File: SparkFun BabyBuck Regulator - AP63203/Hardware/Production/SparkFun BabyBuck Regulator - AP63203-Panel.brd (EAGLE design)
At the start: 151.6 x 179.6 mm, 3156 parts, among them U1 AP63203, U10 AP63203, U100 AP63203, U101 AP63203, U102 AP63203, U103 AP63203, U104 AP63203, U105 AP63203, U106 AP63203, U107 AP63203, U108 AP63203, U109 AP63203, U11 AP63203, U110 AP63203, U111 AP63203, U112 AP63203, U113 AP63203, U114 AP63203, U115 AP63203, U116 AP63203, U117 AP63203, U118 AP63203, U119 AP63203, U12 AP63203, U120 AP63203, U121 AP63203, U122 AP63203, U123 AP63203, U124 AP63203, U125 AP63203, U126 AP63203, U127 AP63203, U128 AP63203, U129 AP63203, U13 AP63203, U130 AP63203, U131 AP63203, U132 AP63203, U133 AP63203, U134 AP63203, U135 AP63203, U136 AP63203, U137 AP63203, U138 AP63203, U139 AP63203, U14 AP63203, U140 AP63203, U141 AP63203, U142 AP63203, U143 AP63203, U144 AP63203, U145 AP63203, U146 AP63203, U147 AP63203, U148 AP63203, U149 AP63203, U15 AP63203, U150 AP63203, U16 AP63203, U17 AP63203, U18 AP63203, U19 AP63203, U2 AP63203, U20 AP63203, U21 AP63203, U22 AP63203, U23 AP63203, U24 AP63203, U25 AP63203, U26 AP63203, U27 AP63203, U28 AP63203, U29 AP63203, U3 AP63203, U30 AP63203, U31 AP63203, U32 AP63203, U33 AP63203, U34 AP63203, U35 AP63203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

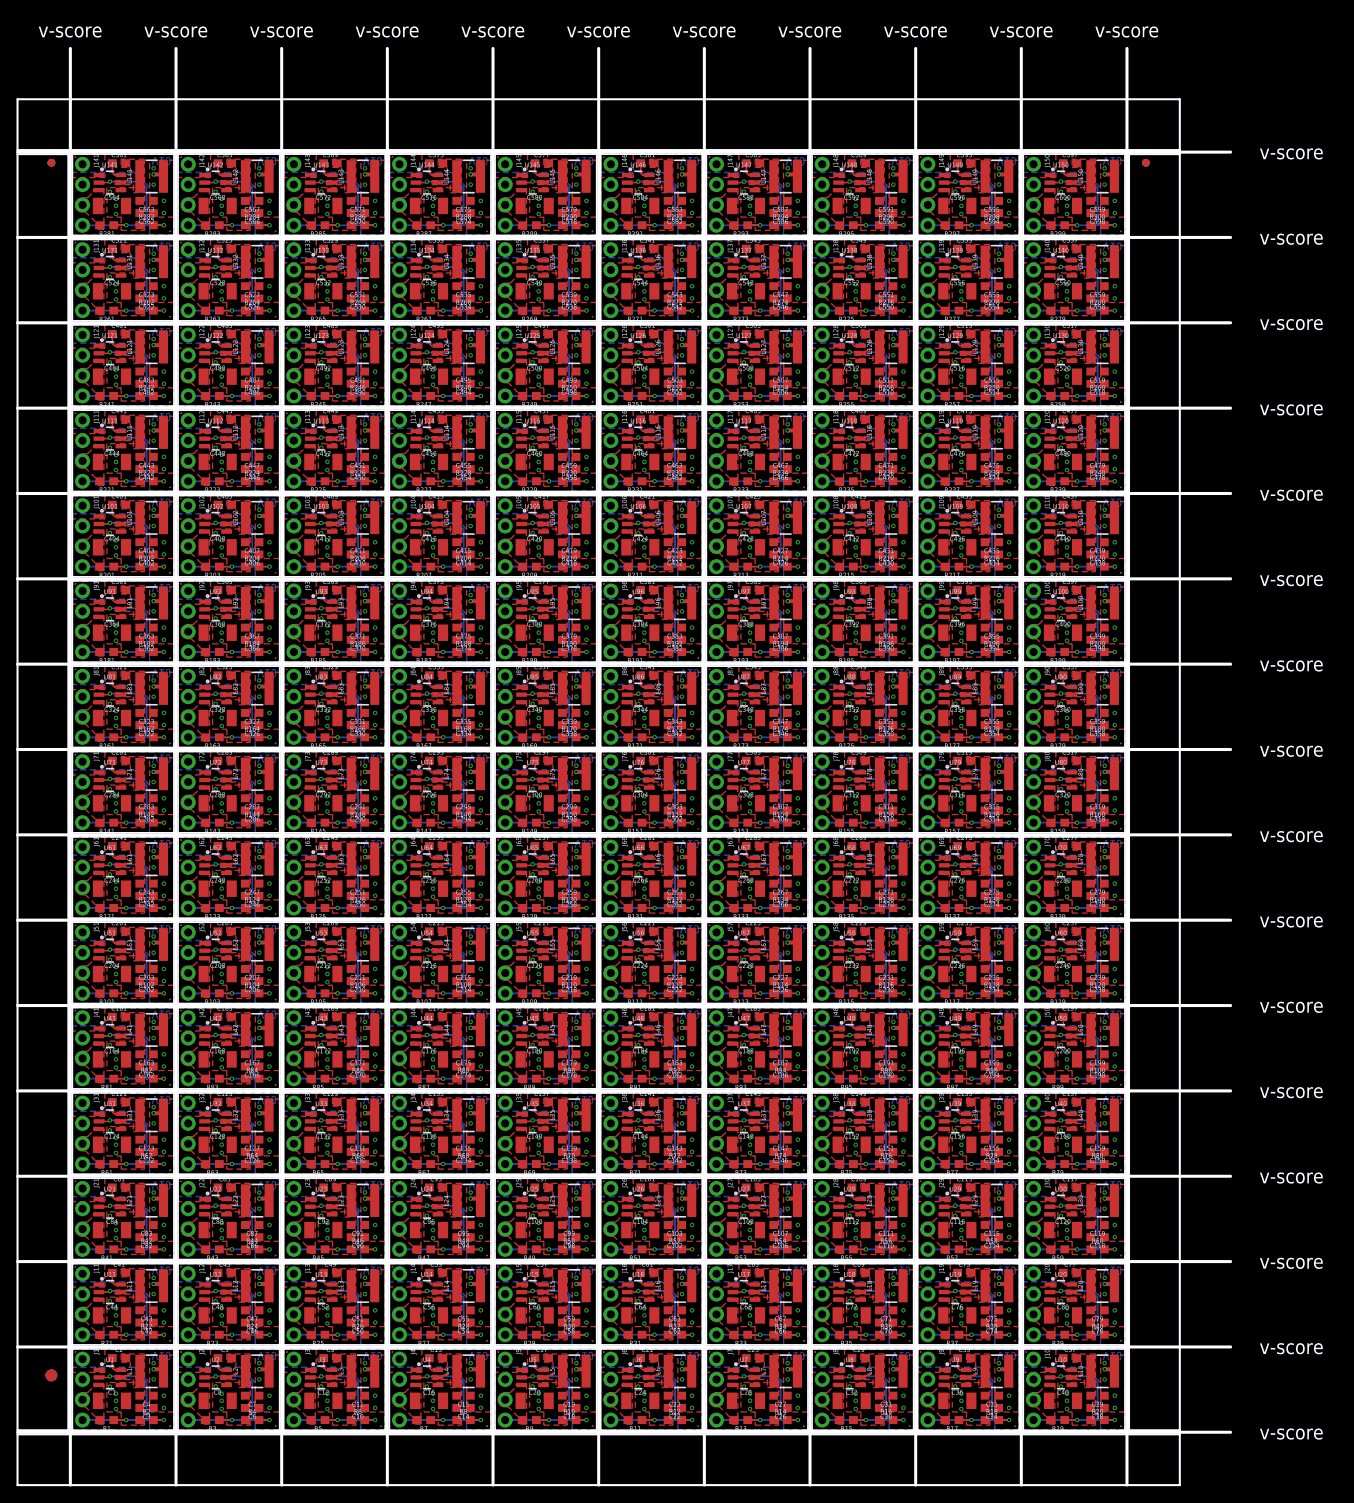
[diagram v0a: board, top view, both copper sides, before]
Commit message: BabyBuck Panel Update
Reduced panel size
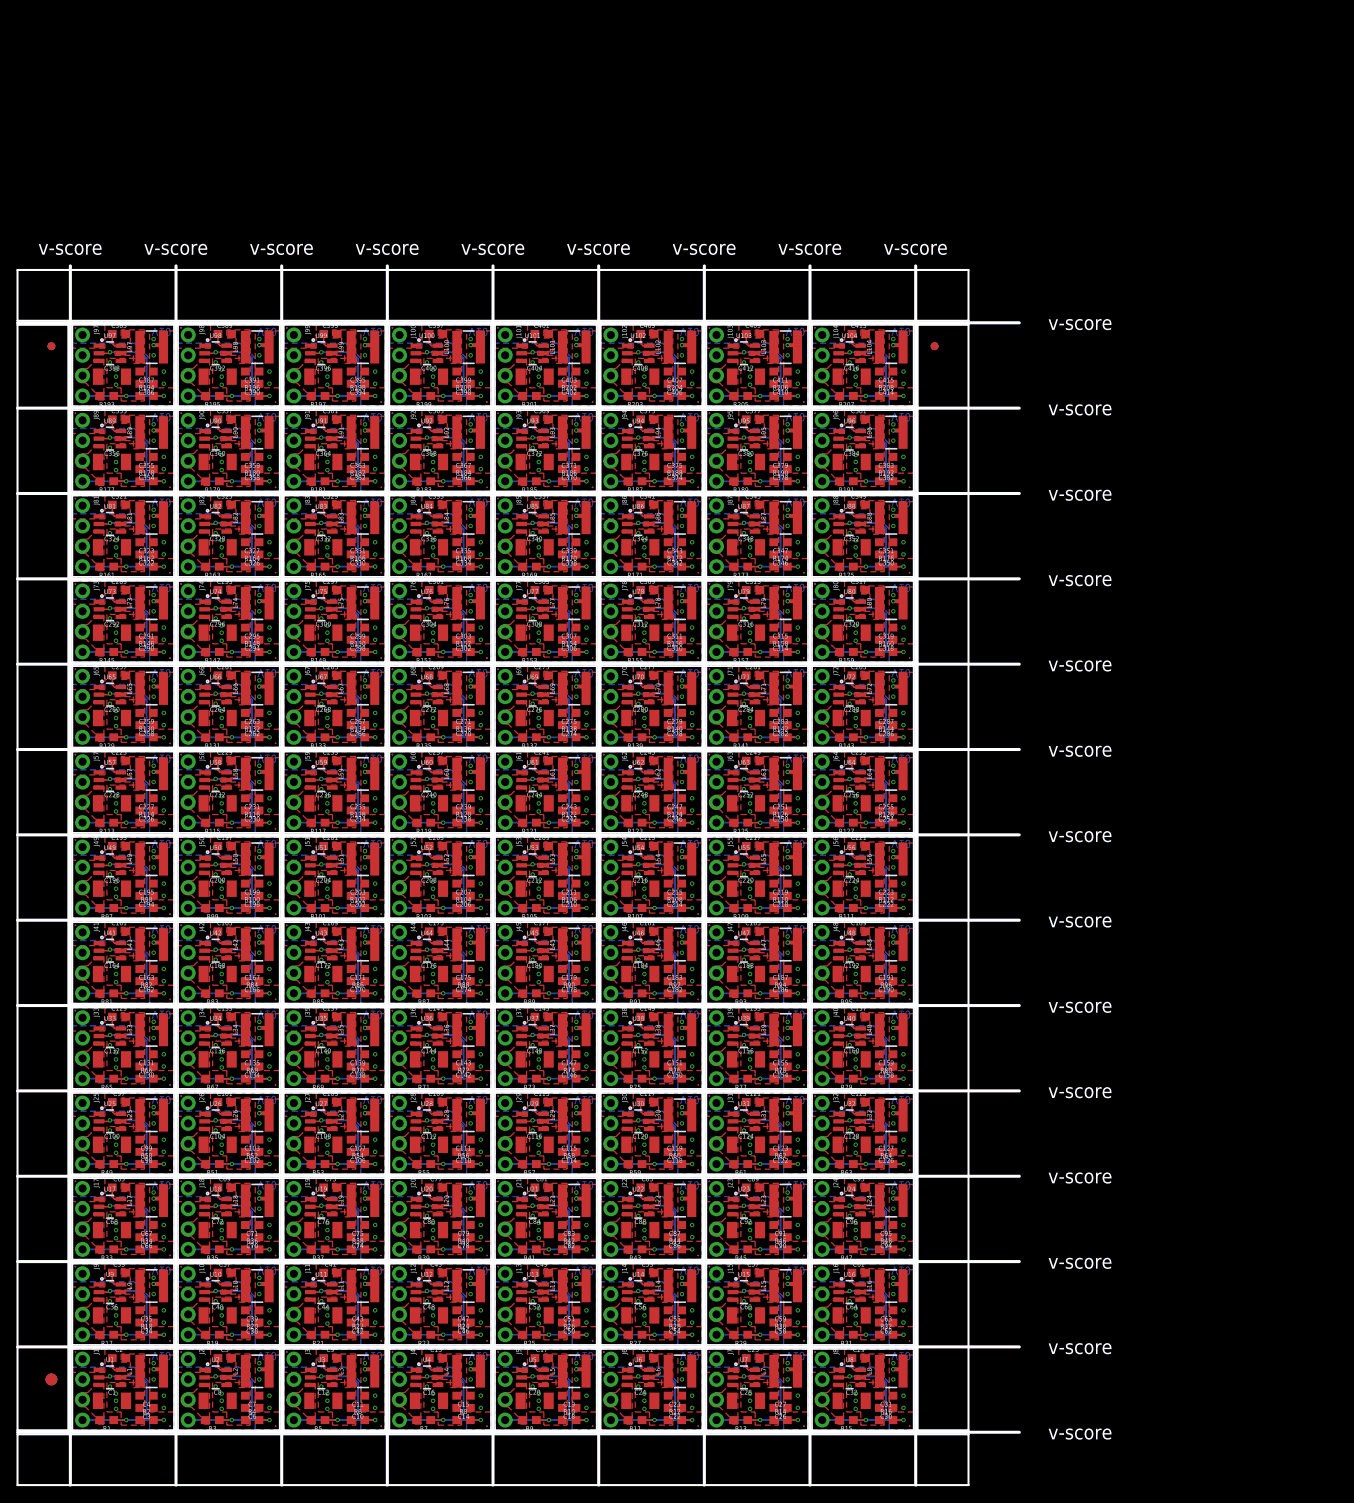
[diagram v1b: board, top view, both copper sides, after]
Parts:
- removed C417, C421, C425, C429, C433, C437, C441, C445, C449, C453, C457, C461, C465, C469, C473, C477, C481, C485, C489, C493, C497, C501, C505, C509, C513, C517, C521, C525, C529, C533, C537, C541, C545, C549, C553, C557, C561, C565, C569, C573, C577, C581, C585, C589, C593, C597: 0.1uF, SparkFun-Capacitors:0603
- removed C418, C419, C422, C423, C426, C427, C430, C431, C434, C435, C438, C439, C442, C443, C446, C447, C450, C451, C454, C455, C458, C459, C462, C463, C466, C467, C470, C471, C474, C475, C478, C479, C482, C483, C486, C487, C490, C491, C494, C495, C498, C499, C502, C503, C506, C507, C510, C511, C514, C515, C518, C519, C522, C523, C526, C527, C530, C531, C534, C535, C538, C539, C542, C543, C546, C547, C550, C551, C554, C555, C558, C559, C562, C563, C566, C567, C570, C571, C574, C575, C578, C579, C582, C583, C586, C587, C590, C591, C594, C595, C598, C599: 22uF, SparkFun-Capacitors:0603
- removed C420, C424, C428, C432, C436, C440, C444, C448, C452, C456, C460, C464, C468, C472, C476, C480, C484, C488, C492, C496, C500, C504, C508, C512, C516, C520, C524, C528, C532, C536, C540, C544, C548, C552, C556, C560, C564, C568, C572, C576, C580, C584, C588, C592, C596, C600: 10uF, SparkFun-Capacitors:1210
- removed FD417, FD418, FD419, FD420, FD421, FD422, FD423, FD424, FD425, FD426, FD427, FD428, FD429, FD430, FD431, FD432, FD433, FD434, FD435, FD436, FD437, FD438, FD439, FD440, FD441, FD442, FD443, FD444, FD445, FD446, FD447, FD448, FD449, FD450, FD451, FD452, FD453, FD454, FD455, FD456, FD457, FD458, FD459, FD460, FD461, FD462, FD463, FD464, FD465, FD466, FD467, FD468, FD469, FD470, FD471, FD472, FD473, FD474, FD475, FD476, FD477, FD478, FD479, FD480, FD481, FD482, FD483, FD484, FD485, FD486, FD487, FD488, FD489, FD490, FD491, FD492, FD493, FD494, FD495, FD496, FD497, FD498, FD499, FD500, FD501, FD502, FD503, FD504, FD505, FD506, FD507, FD508, FD509, FD510, FD511, FD512, FD513, FD514, FD515, FD516, FD517, FD518, FD519, FD520, FD521, FD522, FD523, FD524, FD525, FD526, FD527, FD528, FD529, FD530, FD531, FD532, FD533, FD534, FD535, FD536, FD537, FD538, FD539, FD540, FD541, FD542, FD543, FD544, FD545, FD546, FD547, FD548, FD549, FD550, FD551, FD552, FD553, FD554, FD555, FD556, FD557, FD558, FD559, FD560, FD561, FD562, FD563, FD564, FD565, FD566, FD567, FD568, FD569, FD570, FD571, FD572, FD573, FD574, FD575, FD576, FD577, FD578, FD579, FD580, FD581, FD582, FD583, FD584, FD585, FD586, FD587, FD588, FD589, FD590, FD591, FD592, FD593, FD594, FD595, FD596, FD597, FD598, FD599, FD600: FIDUCIAL0.2MM, SparkFun-Aesthetics:FIDUCIAL-0.2MM
- removed J105, J106, J107, J108, J109, J110, J111, J112, J113, J114, J115, J116, J117, J118, J119, J120, J121, J122, J123, J124, J125, J126, J127, J128, J129, J130, J131, J132, J133, J134, J135, J136, J137, J138, J139, J140, J141, J142, J143, J144, J145, J146, J147, J148, J149, J150: (no value), SparkFun-Connectors:1X04_NO_SILK
- removed L105, L106, L107, L108, L109, L110, L111, L112, L113, L114, L115, L116, L117, L118, L119, L120, L121, L122, L123, L124, L125, L126, L127, L128, L129, L130, L131, L132, L133, L134, L135, L136, L137, L138, L139, L140, L141, L142, L143, L144, L145, L146, L147, L148, L149, L150: 4.7μH, SparkFun-Coils:INDUCTOR_4X4MM
- removed LOGO209, LOGO211, LOGO213, LOGO215, LOGO217, LOGO219, LOGO221, LOGO223, LOGO225, LOGO227, LOGO229, LOGO231, LOGO233, LOGO235, LOGO237, LOGO239, LOGO241, LOGO243, LOGO245, LOGO247, LOGO249, LOGO251, LOGO253, LOGO255, LOGO257, LOGO259, LOGO261, LOGO263, LOGO265, LOGO267, LOGO269, LOGO271, LOGO273, LOGO275, LOGO277, LOGO279, LOGO281, LOGO283, LOGO285, LOGO287, LOGO289, LOGO291, LOGO293, LOGO295, LOGO297, LOGO299: SFE_LOGO_FLAME.1_INCH, SparkFun-Aesthetics:SFE_LOGO_FLAME_.1
- removed LOGO210, LOGO212, LOGO214, LOGO216, LOGO218, LOGO220, LOGO222, LOGO224, LOGO226, LOGO228, LOGO230, LOGO232, LOGO234, LOGO236, LOGO238, LOGO240, LOGO242, LOGO244, LOGO246, LOGO248, LOGO250, LOGO252, LOGO254, LOGO256, LOGO258, LOGO260, LOGO262, LOGO264, LOGO266, LOGO268, LOGO270, LOGO272, LOGO274, LOGO276, LOGO278, LOGO280, LOGO282, LOGO284, LOGO286, LOGO288, LOGO290, LOGO292, LOGO294, LOGO296, LOGO298, LOGO300: OSHW-LOGOS, SparkFun-Aesthetics:OSHW-LOGO-S
- removed R209, R210, R211, R212, R213, R214, R215, R216, R217, R218, R219, R220, R221, R222, R223, R224, R225, R226, R227, R228, R229, R230, R231, R232, R233, R234, R235, R236, R237, R238, R239, R240, R241, R242, R243, R244, R245, R246, R247, R248, R249, R250, R251, R252, R253, R254, R255, R256, R257, R258, R259, R260, R261, R262, R263, R264, R265, R266, R267, R268, R269, R270, R271, R272, R273, R274, R275, R276, R277, R278, R279, R280, R281, R282, R283, R284, R285, R286, R287, R288, R289, R290, R291, R292, R293, R294, R295, R296, R297, R298, R299, R300: 100k, SparkFun-Resistors:0603
- removed U$625, U$631, U$637, U$643, U$649, U$655, U$661, U$667, U$673, U$679, U$685, U$691, U$697, U$703, U$709, U$715, U$721, U$727, U$733, U$739, U$745, U$751, U$757, U$763, U$769, U$775, U$781, U$787, U$793, U$799, U$805, U$811, U$817, U$823, U$829, U$835, U$841, U$847, U$853, U$859, U$865, U$871, U$877, U$883, U$889, U$895: (no value), output:#3V3#0
- removed U$626, U$632, U$638, U$644, U$650, U$656, U$662, U$668, U$674, U$680, U$686, U$692, U$698, U$704, U$710, U$716, U$722, U$728, U$734, U$740, U$746, U$752, U$758, U$764, U$770, U$776, U$782, U$788, U$794, U$800, U$806, U$812, U$818, U$824, U$830, U$836, U$842, U$848, U$854, U$860, U$866, U$872, U$878, U$884, U$890, U$896: (no value), output:#GND#0
- removed U$627, U$633, U$639, U$645, U$651, U$657, U$663, U$669, U$675, U$681, U$687, U$693, U$699, U$705, U$711, U$717, U$723, U$729, U$735, U$741, U$747, U$753, U$759, U$765, U$771, U$777, U$783, U$789, U$795, U$801, U$807, U$813, U$819, U$825, U$831, U$837, U$843, U$849, U$855, U$861, U$867, U$873, U$879, U$885, U$891, U$897: (no value), output:#EN#0
- removed U$628, U$634, U$640, U$646, U$652, U$658, U$664, U$670, U$676, U$682, U$688, U$694, U$700, U$706, U$712, U$718, U$724, U$730, U$736, U$742, U$748, U$754, U$760, U$766, U$772, U$778, U$784, U$790, U$796, U$802, U$808, U$814, U$820, U$826, U$832, U$838, U$844, U$850, U$856, U$862, U$868, U$874, U$880, U$886, U$892, U$898: (no value), output:#VIN#0
- removed U$629, U$635, U$641, U$647, U$653, U$659, U$665, U$671, U$677, U$683, U$689, U$695, U$701, U$707, U$713, U$719, U$725, U$731, U$737, U$743, U$749, U$755, U$761, U$767, U$773, U$779, U$785, U$791, U$797, U$803, U$809, U$815, U$821, U$827, U$833, U$839, U$845, U$851, U$857, U$863, U$869, U$875, U$881, U$887, U$893, U$899: (no value), output:AP632030
- removed U$630, U$636, U$642, U$648, U$654, U$660, U$666, U$672, U$678, U$684, U$690, U$696, U$702, U$708, U$714, U$720, U$726, U$732, U$738, U$744, U$750, U$756, U$762, U$768, U$774, U$780, U$786, U$792, U$798, U$804, U$810, U$816, U$822, U$828, U$834, U$840, U$846, U$852, U$858, U$864, U$870, U$876, U$882, U$888, U$894, U$900: (no value), output:BABYBUCK0
- removed U105, U106, U107, U108, U109, U110, U111, U112, U113, U114, U115, U116, U117, U118, U119, U120, U121, U122, U123, U124, U125, U126, U127, U128, U129, U130, U131, U132, U133, U134, U135, U136, U137, U138, U139, U140, U141, U142, U143, U144, U145, U146, U147, U148, U149, U150: AP63203, SparkFun-IC-Power:SOT23-6
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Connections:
- removed net 3.3V104: C418.1, C419.1, J105.1, L105.P$2, U105.1
- removed net 3.3V105: C422.1, C423.1, J106.1, L106.P$2, U106.1
- removed net 3.3V106: C426.1, C427.1, J107.1, L107.P$2, U107.1
- removed net 3.3V107: C430.1, C431.1, J108.1, L108.P$2, U108.1
- removed net 3.3V108: C434.1, C435.1, J109.1, L109.P$2, U109.1
- removed net 3.3V109: C438.1, C439.1, J110.1, L110.P$2, U110.1
- removed net 3.3V110: C442.1, C443.1, J111.1, L111.P$2, U111.1
- removed net 3.3V111: C446.1, C447.1, J112.1, L112.P$2, U112.1
- removed net 3.3V112: C450.1, C451.1, J113.1, L113.P$2, U113.1
- removed net 3.3V113: C454.1, C455.1, J114.1, L114.P$2, U114.1
- removed net 3.3V114: C458.1, C459.1, J115.1, L115.P$2, U115.1
- removed net 3.3V115: C462.1, C463.1, J116.1, L116.P$2, U116.1
- removed net 3.3V116: C466.1, C467.1, J117.1, L117.P$2, U117.1
- removed net 3.3V117: C470.1, C471.1, J118.1, L118.P$2, U118.1
- removed net 3.3V118: C474.1, C475.1, J119.1, L119.P$2, U119.1
- removed net 3.3V119: C478.1, C479.1, J120.1, L120.P$2, U120.1
- removed net 3.3V120: C482.1, C483.1, J121.1, L121.P$2, U121.1
- removed net 3.3V121: C486.1, C487.1, J122.1, L122.P$2, U122.1
- removed net 3.3V122: C490.1, C491.1, J123.1, L123.P$2, U123.1
- removed net 3.3V123: C494.1, C495.1, J124.1, L124.P$2, U124.1
- removed net 3.3V124: C498.1, C499.1, J125.1, L125.P$2, U125.1
- removed net 3.3V125: C502.1, C503.1, J126.1, L126.P$2, U126.1
- removed net 3.3V126: C506.1, C507.1, J127.1, L127.P$2, U127.1
- removed net 3.3V127: C510.1, C511.1, J128.1, L128.P$2, U128.1
- removed net 3.3V128: C514.1, C515.1, J129.1, L129.P$2, U129.1
- removed net 3.3V129: C518.1, C519.1, J130.1, L130.P$2, U130.1
- removed net 3.3V130: C522.1, C523.1, J131.1, L131.P$2, U131.1
- removed net 3.3V131: C526.1, C527.1, J132.1, L132.P$2, U132.1
- removed net 3.3V132: C530.1, C531.1, J133.1, L133.P$2, U133.1
- removed net 3.3V133: C534.1, C535.1, J134.1, L134.P$2, U134.1
- removed net 3.3V134: C538.1, C539.1, J135.1, L135.P$2, U135.1
- removed net 3.3V135: C542.1, C543.1, J136.1, L136.P$2, U136.1
- removed net 3.3V136: C546.1, C547.1, J137.1, L137.P$2, U137.1
- removed net 3.3V137: C550.1, C551.1, J138.1, L138.P$2, U138.1
- removed net 3.3V138: C554.1, C555.1, J139.1, L139.P$2, U139.1
- removed net 3.3V139: C558.1, C559.1, J140.1, L140.P$2, U140.1
- removed net 3.3V140: C562.1, C563.1, J141.1, L141.P$2, U141.1
- removed net 3.3V141: C566.1, C567.1, J142.1, L142.P$2, U142.1
- removed net 3.3V142: C570.1, C571.1, J143.1, L143.P$2, U143.1
- removed net 3.3V143: C574.1, C575.1, J144.1, L144.P$2, U144.1
- removed net 3.3V144: C578.1, C579.1, J145.1, L145.P$2, U145.1
- removed net 3.3V145: C582.1, C583.1, J146.1, L146.P$2, U146.1
- removed net 3.3V146: C586.1, C587.1, J147.1, L147.P$2, U147.1
- removed net 3.3V147: C590.1, C591.1, J148.1, L148.P$2, U148.1
- removed net 3.3V148: C594.1, C595.1, J149.1, L149.P$2, U149.1
- removed net 3.3V149: C598.1, C599.1, J150.1, L150.P$2, U150.1
- removed net EN104: J105.4, R209.1, R210.2, U105.2
- removed net EN105: J106.4, R211.1, R212.2, U106.2
- removed net EN106: J107.4, R213.1, R214.2, U107.2
- removed net EN107: J108.4, R215.1, R216.2, U108.2
- removed net EN108: J109.4, R217.1, R218.2, U109.2
- removed net EN109: J110.4, R219.1, R220.2, U110.2
- removed net EN110: J111.4, R221.1, R222.2, U111.2
- removed net EN111: J112.4, R223.1, R224.2, U112.2
- removed net EN112: J113.4, R225.1, R226.2, U113.2
- removed net EN113: J114.4, R227.1, R228.2, U114.2
- removed net EN114: J115.4, R229.1, R230.2, U115.2
- removed net EN115: J116.4, R231.1, R232.2, U116.2
- removed net EN116: J117.4, R233.1, R234.2, U117.2
- removed net EN117: J118.4, R235.1, R236.2, U118.2
- removed net EN118: J119.4, R237.1, R238.2, U119.2
- removed net EN119: J120.4, R239.1, R240.2, U120.2
- removed net EN120: J121.4, R241.1, R242.2, U121.2
- removed net EN121: J122.4, R243.1, R244.2, U122.2
- removed net EN122: J123.4, R245.1, R246.2, U123.2
- removed net EN123: J124.4, R247.1, R248.2, U124.2
- removed net EN124: J125.4, R249.1, R250.2, U125.2
- removed net EN125: J126.4, R251.1, R252.2, U126.2
- removed net EN126: J127.4, R253.1, R254.2, U127.2
- removed net EN127: J128.4, R255.1, R256.2, U128.2
- removed net EN128: J129.4, R257.1, R258.2, U129.2
- removed net EN129: J130.4, R259.1, R260.2, U130.2
- removed net EN130: J131.4, R261.1, R262.2, U131.2
- removed net EN131: J132.4, R263.1, R264.2, U132.2
- removed net EN132: J133.4, R265.1, R266.2, U133.2
- removed net EN133: J134.4, R267.1, R268.2, U134.2
- removed net EN134: J135.4, R269.1, R270.2, U135.2
- removed net EN135: J136.4, R271.1, R272.2, U136.2
- removed net EN136: J137.4, R273.1, R274.2, U137.2
- removed net EN137: J138.4, R275.1, R276.2, U138.2
- removed net EN138: J139.4, R277.1, R278.2, U139.2
- removed net EN139: J140.4, R279.1, R280.2, U140.2
- removed net EN140: J141.4, R281.1, R282.2, U141.2
- removed net EN141: J142.4, R283.1, R284.2, U142.2
- removed net EN142: J143.4, R285.1, R286.2, U143.2
- removed net EN143: J144.4, R287.1, R288.2, U144.2
- removed net EN144: J145.4, R289.1, R290.2, U145.2
- removed net EN145: J146.4, R291.1, R292.2, U146.2
- removed net EN146: J147.4, R293.1, R294.2, U147.2
- removed net EN147: J148.4, R295.1, R296.2, U148.2
- removed net EN148: J149.4, R297.1, R298.2, U149.2
- removed net EN149: J150.4, R299.1, R300.2, U150.2
- removed net GND104: C418.2, C419.2, C420.2, J105.2, R210.1, U105.4
- removed net GND105: C422.2, C423.2, C424.2, J106.2, R212.1, U106.4
- removed net GND106: C426.2, C427.2, C428.2, J107.2, R214.1, U107.4
- removed net GND107: C430.2, C431.2, C432.2, J108.2, R216.1, U108.4
- removed net GND108: C434.2, C435.2, C436.2, J109.2, R218.1, U109.4
- removed net GND109: C438.2, C439.2, C440.2, J110.2, R220.1, U110.4
- removed net GND110: C442.2, C443.2, C444.2, J111.2, R222.1, U111.4
- removed net GND111: C446.2, C447.2, C448.2, J112.2, R224.1, U112.4
- removed net GND112: C450.2, C451.2, C452.2, J113.2, R226.1, U113.4
- removed net GND113: C454.2, C455.2, C456.2, J114.2, R228.1, U114.4
- removed net GND114: C458.2, C459.2, C460.2, J115.2, R230.1, U115.4
- removed net GND115: C462.2, C463.2, C464.2, J116.2, R232.1, U116.4
- removed net GND116: C466.2, C467.2, C468.2, J117.2, R234.1, U117.4
- removed net GND117: C470.2, C471.2, C472.2, J118.2, R236.1, U118.4
- removed net GND118: C474.2, C475.2, C476.2, J119.2, R238.1, U119.4
- removed net GND119: C478.2, C479.2, C480.2, J120.2, R240.1, U120.4
- removed net GND120: C482.2, C483.2, C484.2, J121.2, R242.1, U121.4
- removed net GND121: C486.2, C487.2, C488.2, J122.2, R244.1, U122.4
- removed net GND122: C490.2, C491.2, C492.2, J123.2, R246.1, U123.4
- removed net GND123: C494.2, C495.2, C496.2, J124.2, R248.1, U124.4
- removed net GND124: C498.2, C499.2, C500.2, J125.2, R250.1, U125.4
- removed net GND125: C502.2, C503.2, C504.2, J126.2, R252.1, U126.4
- removed net GND126: C506.2, C507.2, C508.2, J127.2, R254.1, U127.4
- removed net GND127: C510.2, C511.2, C512.2, J128.2, R256.1, U128.4
- removed net GND128: C514.2, C515.2, C516.2, J129.2, R258.1, U129.4
- removed net GND129: C518.2, C519.2, C520.2, J130.2, R260.1, U130.4
- removed net GND130: C522.2, C523.2, C524.2, J131.2, R262.1, U131.4
- removed net GND131: C526.2, C527.2, C528.2, J132.2, R264.1, U132.4
- removed net GND132: C530.2, C531.2, C532.2, J133.2, R266.1, U133.4
- removed net GND133: C534.2, C535.2, C536.2, J134.2, R268.1, U134.4
- removed net GND134: C538.2, C539.2, C540.2, J135.2, R270.1, U135.4
- removed net GND135: C542.2, C543.2, C544.2, J136.2, R272.1, U136.4
- removed net GND136: C546.2, C547.2, C548.2, J137.2, R274.1, U137.4
- removed net GND137: C550.2, C551.2, C552.2, J138.2, R276.1, U138.4
- removed net GND138: C554.2, C555.2, C556.2, J139.2, R278.1, U139.4
- removed net GND139: C558.2, C559.2, C560.2, J140.2, R280.1, U140.4
- removed net GND140: C562.2, C563.2, C564.2, J141.2, R282.1, U141.4
- removed net GND141: C566.2, C567.2, C568.2, J142.2, R284.1, U142.4
- removed net GND142: C570.2, C571.2, C572.2, J143.2, R286.1, U143.4
- removed net GND143: C574.2, C575.2, C576.2, J144.2, R288.1, U144.4
- removed net GND144: C578.2, C579.2, C580.2, J145.2, R290.1, U145.4
- removed net GND145: C582.2, C583.2, C584.2, J146.2, R292.1, U146.4
- removed net GND146: C586.2, C587.2, C588.2, J147.2, R294.1, U147.4
- removed net GND147: C590.2, C591.2, C592.2, J148.2, R296.1, U148.4
- removed net GND148: C594.2, C595.2, C596.2, J149.2, R298.1, U149.4
- removed net GND149: C598.2, C599.2, C600.2, J150.2, R300.1, U150.4
- removed net N$209: C417.1, U105.6
- removed net N$210: C417.2, L105.P$1, U105.5
- removed net N$211: C421.1, U106.6
- removed net N$212: C421.2, L106.P$1, U106.5
- removed net N$213: C425.1, U107.6
- removed net N$214: C425.2, L107.P$1, U107.5
- removed net N$215: C429.1, U108.6
- removed net N$216: C429.2, L108.P$1, U108.5
- removed net N$217: C433.1, U109.6
- removed net N$218: C433.2, L109.P$1, U109.5
- removed net N$219: C437.1, U110.6
- removed net N$220: C437.2, L110.P$1, U110.5
- removed net N$221: C441.1, U111.6
- removed net N$222: C441.2, L111.P$1, U111.5
- removed net N$223: C445.1, U112.6
- removed net N$224: C445.2, L112.P$1, U112.5
- removed net N$225: C449.1, U113.6
- removed net N$226: C449.2, L113.P$1, U113.5
- removed net N$227: C453.1, U114.6
- removed net N$228: C453.2, L114.P$1, U114.5
- removed net N$229: C457.1, U115.6
- removed net N$230: C457.2, L115.P$1, U115.5
- removed net N$231: C461.1, U116.6
- removed net N$232: C461.2, L116.P$1, U116.5
- removed net N$233: C465.1, U117.6
- removed net N$234: C465.2, L117.P$1, U117.5
- removed net N$235: C469.1, U118.6
- removed net N$236: C469.2, L118.P$1, U118.5
- removed net N$237: C473.1, U119.6
- removed net N$238: C473.2, L119.P$1, U119.5
- removed net N$239: C477.1, U120.6
- removed net N$240: C477.2, L120.P$1, U120.5
- removed net N$241: C481.1, U121.6
- removed net N$242: C481.2, L121.P$1, U121.5
- removed net N$243: C485.1, U122.6
- removed net N$244: C485.2, L122.P$1, U122.5
- removed net N$245: C489.1, U123.6
- removed net N$246: C489.2, L123.P$1, U123.5
- removed net N$247: C493.1, U124.6
- removed net N$248: C493.2, L124.P$1, U124.5
- removed net N$249: C497.1, U125.6
- removed net N$250: C497.2, L125.P$1, U125.5
- removed net N$251: C501.1, U126.6
- removed net N$252: C501.2, L126.P$1, U126.5
- removed net N$253: C505.1, U127.6
- removed net N$254: C505.2, L127.P$1, U127.5
- removed net N$255: C509.1, U128.6
- removed net N$256: C509.2, L128.P$1, U128.5
- removed net N$257: C513.1, U129.6
- removed net N$258: C513.2, L129.P$1, U129.5
- removed net N$259: C517.1, U130.6
- removed net N$260: C517.2, L130.P$1, U130.5
- removed net N$261: C521.1, U131.6
- removed net N$262: C521.2, L131.P$1, U131.5
- removed net N$263: C525.1, U132.6
- removed net N$264: C525.2, L132.P$1, U132.5
- removed net N$265: C529.1, U133.6
- removed net N$266: C529.2, L133.P$1, U133.5
- removed net N$267: C533.1, U134.6
- removed net N$268: C533.2, L134.P$1, U134.5
- removed net N$269: C537.1, U135.6
- removed net N$270: C537.2, L135.P$1, U135.5
- removed net N$271: C541.1, U136.6
- removed net N$272: C541.2, L136.P$1, U136.5
- removed net N$273: C545.1, U137.6
- removed net N$274: C545.2, L137.P$1, U137.5
- removed net N$275: C549.1, U138.6
- removed net N$276: C549.2, L138.P$1, U138.5
- removed net N$277: C553.1, U139.6
- removed net N$278: C553.2, L139.P$1, U139.5
- removed net N$279: C557.1, U140.6
- removed net N$280: C557.2, L140.P$1, U140.5
- removed net N$281: C561.1, U141.6
- removed net N$282: C561.2, L141.P$1, U141.5
- removed net N$283: C565.1, U142.6
- removed net N$284: C565.2, L142.P$1, U142.5
- removed net N$285: C569.1, U143.6
- removed net N$286: C569.2, L143.P$1, U143.5
- removed net N$287: C573.1, U144.6
- removed net N$288: C573.2, L144.P$1, U144.5
- removed net N$289: C577.1, U145.6
- removed net N$290: C577.2, L145.P$1, U145.5
- removed net N$291: C581.1, U146.6
- removed net N$292: C581.2, L146.P$1, U146.5
- removed net N$293: C585.1, U147.6
- removed net N$294: C585.2, L147.P$1, U147.5
- removed net N$295: C589.1, U148.6
- removed net N$296: C589.2, L148.P$1, U148.5
- removed net N$297: C593.1, U149.6
- removed net N$298: C593.2, L149.P$1, U149.5
- removed net N$299: C597.1, U150.6
- removed net N$300: C597.2, L150.P$1, U150.5
- removed net VIN104: C420.1, J105.3, R209.2, U105.3
- removed net VIN105: C424.1, J106.3, R211.2, U106.3
- removed net VIN106: C428.1, J107.3, R213.2, U107.3
- removed net VIN107: C432.1, J108.3, R215.2, U108.3
- removed net VIN108: C436.1, J109.3, R217.2, U109.3
- removed net VIN109: C440.1, J110.3, R219.2, U110.3
- removed net VIN110: C444.1, J111.3, R221.2, U111.3
- removed net VIN111: C448.1, J112.3, R223.2, U112.3
- removed net VIN112: C452.1, J113.3, R225.2, U113.3
- removed net VIN113: C456.1, J114.3, R227.2, U114.3
- removed net VIN114: C460.1, J115.3, R229.2, U115.3
- removed net VIN115: C464.1, J116.3, R231.2, U116.3
- removed net VIN116: C468.1, J117.3, R233.2, U117.3
- removed net VIN117: C472.1, J118.3, R235.2, U118.3
- removed net VIN118: C476.1, J119.3, R237.2, U119.3
- removed net VIN119: C480.1, J120.3, R239.2, U120.3
- removed net VIN120: C484.1, J121.3, R241.2, U121.3
- removed net VIN121: C488.1, J122.3, R243.2, U122.3
- removed net VIN122: C492.1, J123.3, R245.2, U123.3
- removed net VIN123: C496.1, J124.3, R247.2, U124.3
- removed net VIN124: C500.1, J125.3, R249.2, U125.3
- removed net VIN125: C504.1, J126.3, R251.2, U126.3
- removed net VIN126: C508.1, J127.3, R253.2, U127.3
- removed net VIN127: C512.1, J128.3, R255.2, U128.3
- removed net VIN128: C516.1, J129.3, R257.2, U129.3
- removed net VIN129: C520.1, J130.3, R259.2, U130.3
- removed net VIN130: C524.1, J131.3, R261.2, U131.3
- removed net VIN131: C528.1, J132.3, R263.2, U132.3
- removed net VIN132: C532.1, J133.3, R265.2, U133.3
- removed net VIN133: C536.1, J134.3, R267.2, U134.3
- removed net VIN134: C540.1, J135.3, R269.2, U135.3
- removed net VIN135: C544.1, J136.3, R271.2, U136.3
- removed net VIN136: C548.1, J137.3, R273.2, U137.3
- removed net VIN137: C552.1, J138.3, R275.2, U138.3
- removed net VIN138: C556.1, J139.3, R277.2, U139.3
- removed net VIN139: C560.1, J140.3, R279.2, U140.3
- removed net VIN140: C564.1, J141.3, R281.2, U141.3
- removed net VIN141: C568.1, J142.3, R283.2, U142.3
- removed net VIN142: C572.1, J143.3, R285.2, U143.3
- removed net VIN143: C576.1, J144.3, R287.2, U144.3
- removed net VIN144: C580.1, J145.3, R289.2, U145.3
- removed net VIN145: C584.1, J146.3, R291.2, U146.3
- removed net VIN146: C588.1, J147.3, R293.2, U147.3
- removed net VIN147: C592.1, J148.3, R295.2, U148.3
- removed net VIN148: C596.1, J149.3, R297.2, U149.3
- removed net VIN149: C600.1, J150.3, R299.2, U150.3
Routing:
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- removed copper zone on layer 1, net 3.3V104
- removed copper zone on layer 16, net 3.3V104
- removed copper zone on layer 1, net 3.3V105
- removed copper zone on layer 16, net 3.3V105
- removed copper zone on layer 1, net 3.3V106
- removed copper zone on layer 16, net 3.3V106
- removed copper zone on layer 1, net 3.3V107
- removed copper zone on layer 16, net 3.3V107
- removed copper zone on layer 1, net 3.3V108
- removed copper zone on layer 16, net 3.3V108
- removed copper zone on layer 1, net 3.3V109
- removed copper zone on layer 16, net 3.3V109
- removed copper zone on layer 1, net 3.3V110
- removed copper zone on layer 16, net 3.3V110
- removed copper zone on layer 1, net 3.3V111
- removed copper zone on layer 16, net 3.3V111
- removed copper zone on layer 1, net 3.3V112
- removed copper zone on layer 16, net 3.3V112
- removed copper zone on layer 1, net 3.3V113
- removed copper zone on layer 16, net 3.3V113
- removed copper zone on layer 1, net 3.3V114
- removed copper zone on layer 16, net 3.3V114
- removed copper zone on layer 1, net 3.3V115
- removed copper zone on layer 16, net 3.3V115
- removed copper zone on layer 1, net 3.3V116
- removed copper zone on layer 16, net 3.3V116
- removed copper zone on layer 1, net 3.3V117
- removed copper zone on layer 16, net 3.3V117
- removed copper zone on layer 1, net 3.3V118
- removed copper zone on layer 16, net 3.3V118
- removed copper zone on layer 1, net 3.3V119
- removed copper zone on layer 16, net 3.3V119
- removed copper zone on layer 1, net 3.3V120
- removed copper zone on layer 16, net 3.3V120
- removed copper zone on layer 1, net 3.3V121
- removed copper zone on layer 16, net 3.3V121
- removed copper zone on layer 1, net 3.3V122
- removed copper zone on layer 16, net 3.3V122
- removed copper zone on layer 1, net 3.3V123
- removed copper zone on layer 16, net 3.3V123
- removed copper zone on layer 1, net 3.3V124
- removed copper zone on layer 16, net 3.3V124
- removed copper zone on layer 1, net 3.3V125
- removed copper zone on layer 16, net 3.3V125
- removed copper zone on layer 1, net 3.3V126
- removed copper zone on layer 16, net 3.3V126
- removed copper zone on layer 1, net 3.3V127
- removed copper zone on layer 16, net 3.3V127
- removed copper zone on layer 1, net 3.3V128
- removed copper zone on layer 16, net 3.3V128
- removed copper zone on layer 1, net 3.3V129
- removed copper zone on layer 16, net 3.3V129
- removed copper zone on layer 1, net 3.3V130
- removed copper zone on layer 16, net 3.3V130
- removed copper zone on layer 1, net 3.3V131
- removed copper zone on layer 16, net 3.3V131
- removed copper zone on layer 1, net 3.3V132
- removed copper zone on layer 16, net 3.3V132
- removed copper zone on layer 1, net 3.3V133
- removed copper zone on layer 16, net 3.3V133
- removed copper zone on layer 1, net 3.3V134
- removed copper zone on layer 16, net 3.3V134
- removed copper zone on layer 1, net 3.3V135
- removed copper zone on layer 16, net 3.3V135
- removed copper zone on layer 1, net 3.3V136
- removed copper zone on layer 16, net 3.3V136
- removed copper zone on layer 1, net 3.3V137
- removed copper zone on layer 16, net 3.3V137
- removed copper zone on layer 1, net 3.3V138
- removed copper zone on layer 16, net 3.3V138
- removed copper zone on layer 1, net 3.3V139
- removed copper zone on layer 16, net 3.3V139
- removed copper zone on layer 1, net 3.3V140
- removed copper zone on layer 16, net 3.3V140
- removed copper zone on layer 1, net 3.3V141
- removed copper zone on layer 16, net 3.3V141
- removed copper zone on layer 1, net 3.3V142
- removed copper zone on layer 16, net 3.3V142
- removed copper zone on layer 1, net 3.3V143
- removed copper zone on layer 16, net 3.3V143
- removed copper zone on layer 1, net 3.3V144
- removed copper zone on layer 16, net 3.3V144
- removed copper zone on layer 1, net 3.3V145
- removed copper zone on layer 16, net 3.3V145
- removed copper zone on layer 1, net 3.3V146
- removed copper zone on layer 16, net 3.3V146
- removed copper zone on layer 1, net 3.3V147
- removed copper zone on layer 16, net 3.3V147
- removed copper zone on layer 1, net 3.3V148
- removed copper zone on layer 16, net 3.3V148
- removed copper zone on layer 1, net 3.3V149
- removed copper zone on layer 16, net 3.3V149
- removed copper zone on layer 1, net GND104
- removed copper zone on layer 16, net GND104
- removed copper zone on layer 1, net GND105
- removed copper zone on layer 16, net GND105
- removed copper zone on layer 1, net GND106
- removed copper zone on layer 16, net GND106
- removed copper zone on layer 1, net GND107
- removed copper zone on layer 16, net GND107
- removed copper zone on layer 1, net GND108
- removed copper zone on layer 16, net GND108
- removed copper zone on layer 1, net GND109
- removed copper zone on layer 16, net GND109
- removed copper zone on layer 1, net GND110
- removed copper zone on layer 16, net GND110
- removed copper zone on layer 1, net GND111
- removed copper zone on layer 16, net GND111
- removed copper zone on layer 1, net GND112
- removed copper zone on layer 16, net GND112
- removed copper zone on layer 1, net GND113
- removed copper zone on layer 16, net GND113
- removed copper zone on layer 1, net GND114
- removed copper zone on layer 16, net GND114
- removed copper zone on layer 1, net GND115
- removed copper zone on layer 16, net GND115
- removed copper zone on layer 1, net GND116
- removed copper zone on layer 16, net GND116
- removed copper zone on layer 1, net GND117
- removed copper zone on layer 16, net GND117
- removed copper zone on layer 1, net GND118
- removed copper zone on layer 16, net GND118
- removed copper zone on layer 1, net GND119
- removed copper zone on layer 16, net GND119
- removed copper zone on layer 1, net GND120
- removed copper zone on layer 16, net GND120
- removed copper zone on layer 1, net GND121
- removed copper zone on layer 16, net GND121
- removed copper zone on layer 1, net GND122
- removed copper zone on layer 16, net GND122
- removed copper zone on layer 1, net GND123
- removed copper zone on layer 16, net GND123
- removed copper zone on layer 1, net GND124
- removed copper zone on layer 16, net GND124
- removed copper zone on layer 1, net GND125
- removed copper zone on layer 16, net GND125
- removed copper zone on layer 1, net GND126
- removed copper zone on layer 16, net GND126
- removed copper zone on layer 1, net GND127
- removed copper zone on layer 16, net GND127
- removed copper zone on layer 1, net GND128
- removed copper zone on layer 16, net GND128
- removed copper zone on layer 1, net GND129
- removed copper zone on layer 16, net GND129
- removed copper zone on layer 1, net GND130
- removed copper zone on layer 16, net GND130
- removed copper zone on layer 1, net GND131
- removed copper zone on layer 16, net GND131
- removed copper zone on layer 1, net GND132
- removed copper zone on layer 16, net GND132
- removed copper zone on layer 1, net GND133
- removed copper zone on layer 16, net GND133
- removed copper zone on layer 1, net GND134
- removed copper zone on layer 16, net GND134
- removed copper zone on layer 1, net GND135
- removed copper zone on layer 16, net GND135
- removed copper zone on layer 1, net GND136
- removed copper zone on layer 16, net GND136
- removed copper zone on layer 1, net GND137
- removed copper zone on layer 16, net GND137
- removed copper zone on layer 1, net GND138
- removed copper zone on layer 16, net GND138
- removed copper zone on layer 1, net GND139
- removed copper zone on layer 16, net GND139
- removed copper zone on layer 1, net GND140
- removed copper zone on layer 16, net GND140
- removed copper zone on layer 1, net GND141
- removed copper zone on layer 16, net GND141
- removed copper zone on layer 1, net GND142
- removed copper zone on layer 16, net GND142
- removed copper zone on layer 1, net GND143
- removed copper zone on layer 16, net GND143
- removed copper zone on layer 1, net GND144
- removed copper zone on layer 16, net GND144
- removed copper zone on layer 1, net GND145
- removed copper zone on layer 16, net GND145
- removed copper zone on layer 1, net GND146
- removed copper zone on layer 16, net GND146
- removed copper zone on layer 1, net GND147
- removed copper zone on layer 16, net GND147
- removed copper zone on layer 1, net GND148
- removed copper zone on layer 16, net GND148
- removed copper zone on layer 1, net GND149
- removed copper zone on layer 16, net GND149
- removed copper zone on layer 1, net N$210
- removed copper zone on layer 1, net N$212
- removed copper zone on layer 1, net N$214
- removed copper zone on layer 1, net N$216
- removed copper zone on layer 1, net N$218
- removed copper zone on layer 1, net N$220
- removed copper zone on layer 1, net N$222
- removed copper zone on layer 1, net N$224
- removed copper zone on layer 1, net N$226
- removed copper zone on layer 1, net N$228
- removed copper zone on layer 1, net N$230
- removed copper zone on layer 1, net N$232
- removed copper zone on layer 1, net N$234
- removed copper zone on layer 1, net N$236
- removed copper zone on layer 1, net N$238
- removed copper zone on layer 1, net N$240
- removed copper zone on layer 1, net N$242
- removed copper zone on layer 1, net N$244
- removed copper zone on layer 1, net N$246
- removed copper zone on layer 1, net N$248
- removed copper zone on layer 1, net N$250
- removed copper zone on layer 1, net N$252
- removed copper zone on layer 1, net N$254
- removed copper zone on layer 1, net N$256
- removed copper zone on layer 1, net N$258
- removed copper zone on layer 1, net N$260
- removed copper zone on layer 1, net N$262
- removed copper zone on layer 1, net N$264
- removed copper zone on layer 1, net N$266
- removed copper zone on layer 1, net N$268
- removed copper zone on layer 1, net N$270
- removed copper zone on layer 1, net N$272
- removed copper zone on layer 1, net N$274
- removed copper zone on layer 1, net N$276
- removed copper zone on layer 1, net N$278
- removed copper zone on layer 1, net N$280
- removed copper zone on layer 1, net N$282
- removed copper zone on layer 1, net N$284
- removed copper zone on layer 1, net N$286
- removed copper zone on layer 1, net N$288
- removed copper zone on layer 1, net N$290
- removed copper zone on layer 1, net N$292
- removed copper zone on layer 1, net N$294
- removed copper zone on layer 1, net N$296
- removed copper zone on layer 1, net N$298
- removed copper zone on layer 1, net N$300
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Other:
- board size 151.6 x 179.6 mm -> 125.2 x 152.4 mm
